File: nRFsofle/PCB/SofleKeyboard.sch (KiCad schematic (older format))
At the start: 106 parts, among them J1 LED, J2 4PIN, J3 OLED, J4 key leds, J5 backlight sel, J6 indicator bypass, J7 JST_Micro_2, J8 OLED, P1 i2c_pin, P2 i2c_pin, SW1 SW_PUSH-MX_W_LED, SW10 SW_PUSH-MX_W_LED, SW11 SW_PUSH-MX_W_LED, SW12 SW_PUSH-MX_W_LED, SW13 SW_PUSH-MX_W_LED, SW14 SW_PUSH-MX_W_LED, SW15 SW_PUSH-MX_W_LED, SW16 SW_PUSH-MX_W_LED, SW17 SW_PUSH-MX_W_LED, SW18 SW_PUSH-MX_W_LED, SW19 SW_PUSH-MX_W_LED, SW2 SW_PUSH-MX_W_LED, SW20 SW_PUSH-MX_W_LED, SW21 SW_PUSH-MX_W_LED, SW22 SW_PUSH-MX_W_LED, SW23 SW_PUSH-MX_W_LED, SW24 SW_PUSH-MX_W_LED, SW25 Rotary_Encoder_Switch, SW26 SW_PUSH-MX_W_LED, SW27 SW_PUSH-MX_W_LED, SW28 SW_PUSH-MX_W_LED, SW29 SW_PUSH-MX_W_LED, SW3 SW_PUSH-MX_W_LED, SW30 SW_PUSH-MX_W_LED, SW31 SPDT_Switch, SW4 SW_PUSH-MX_W_LED, SW5 SW_PUSH-MX_W_LED, SW6 SW_PUSH-MX_W_LED, SW7 SW_PUSH-MX_W_LED, SW8 SW_PUSH-MX_W_LED, SW9 SW_PUSH-MX_W_LED, U1 nRFMicro

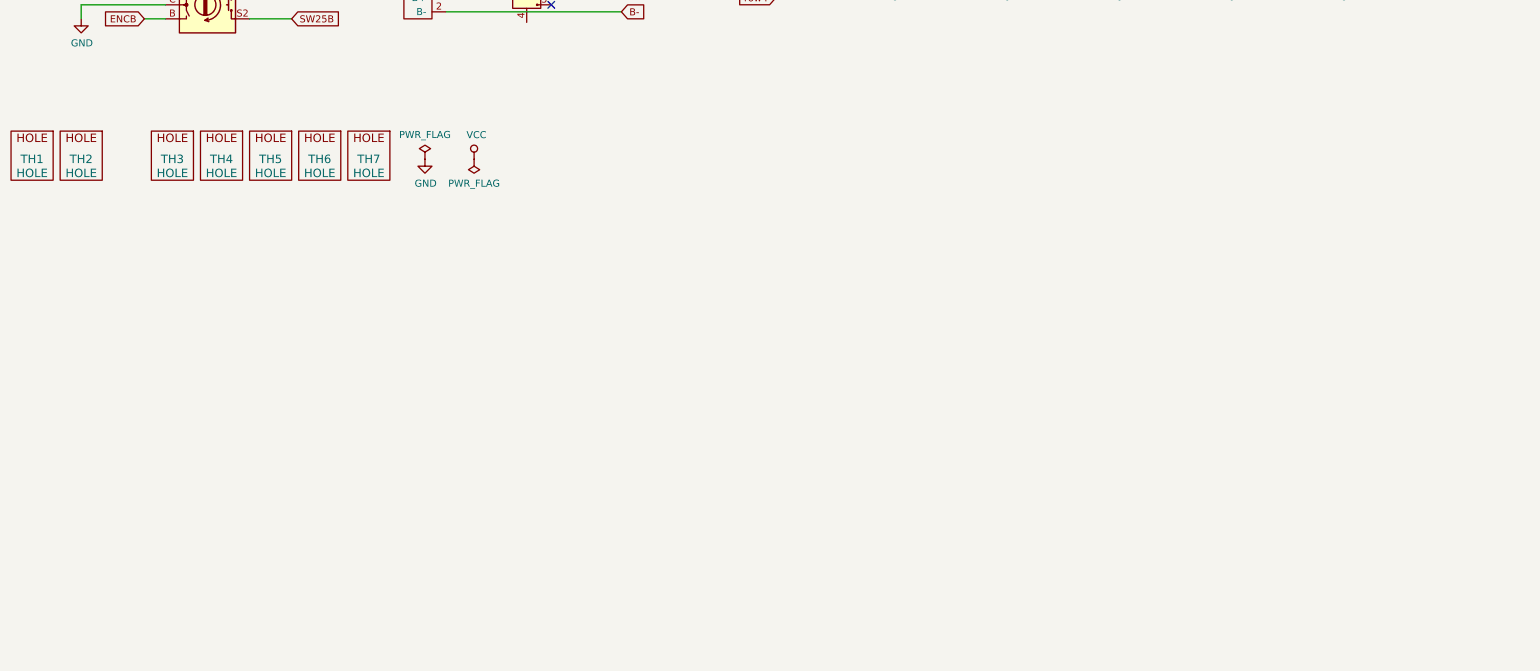
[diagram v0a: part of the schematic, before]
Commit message: Implemented the schematic to add fingerprint sensor
The implemented circuit is duplicated to put the circuit in both layers,
so the board can be printed for both sides of the keyboard.
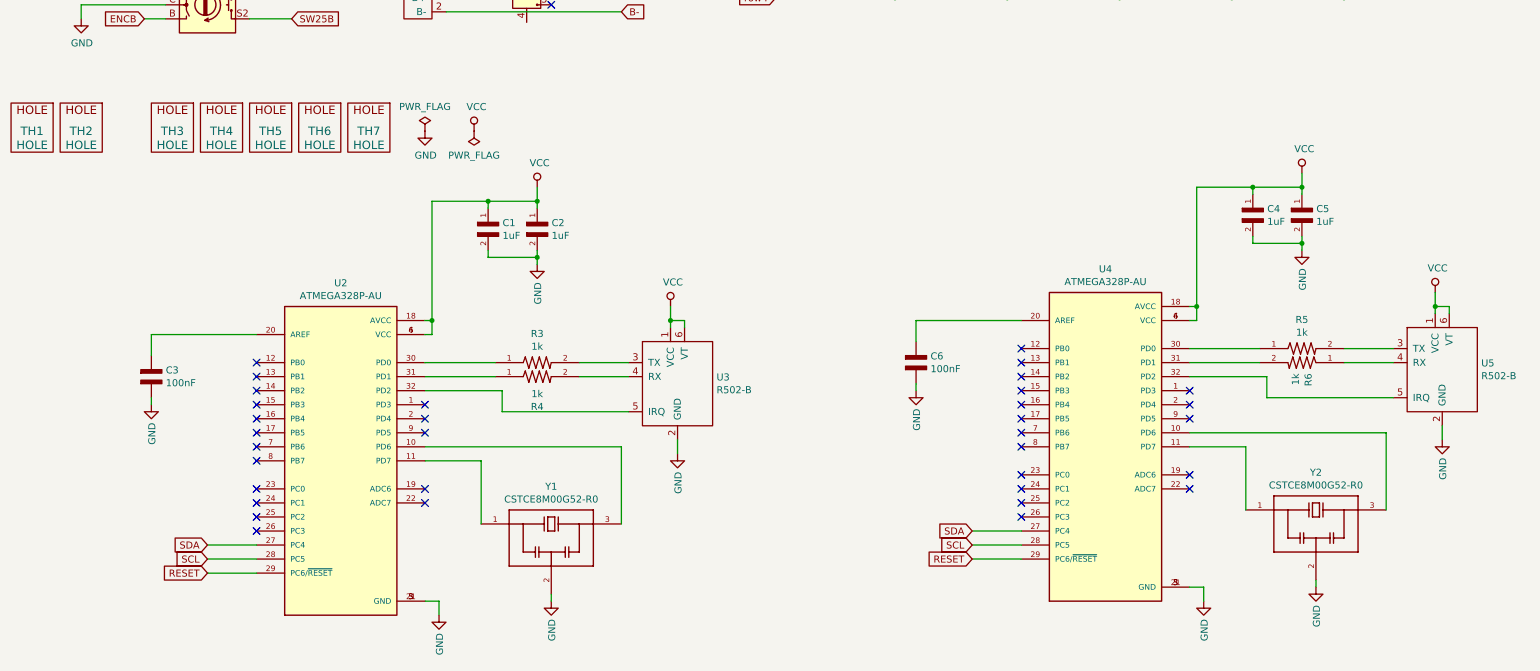
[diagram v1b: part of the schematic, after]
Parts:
- added C1, C2, C4, C5: 1uF, 1uF, symbol Additions:1uF
- added C3, C6: 100nF, 100nF, symbol Additions:100nF
- added R3, R4, R5, R6: 1k, 1k, symbol Additions:1k
- added U2, U4: ATMEGA328P-AU, QFP80P900X900X120-32N, symbol Additions:ATMEGA328P-AU
- added U3, U5: R502-B, symbol Additions:R502-B
- added Y1, Y2: CSTCE8M00G52-R0, OSC_CSTCE8M00G52-R0, symbol Additions:CSTCE8M00G52-R0
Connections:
- net GND: now also C1.2, C2.2, C3.1, C4.2, C5.2, C6.1, U2.21 (GND), U2.3 (GND), U2.5 (GND), U3.2 (GND), U4.21 (GND), U4.3 (GND), U4.5 (GND), U5.2 (GND), Y1.2, Y2.2
- net RESET: now also U2.29 (PC6/~RESET), U4.29 (PC6/~RESET)
- net SCL: now also U2.28 (PC5), U4.28 (PC5)
- net SDA: now also U2.27 (PC4), U4.27 (PC4)
- net VCC: now also C1.1, C2.1, C4.1, C5.1, U2.18 (AVCC), U2.4 (VCC), U2.6 (VCC), U3.1 (VCC), U3.6 (VT), U4.18 (AVCC), U4.4 (VCC), U4.6 (VCC), U5.1 (VCC), U5.6 (VT)
- new net: U2.10 (PD6), Y1.3
- new net: U2.11 (PD7), Y1.1
- new net: C3.2, U2.20 (AREF)
- new net: R3.1, U2.30 (PD0)
- new net: R4.1, U2.31 (PD1)
- new net: U2.32 (PD2), U3.5 (IRQ)
- new net: R3.2, U3.3 (TX)
- new net: R4.2, U3.4 (RX)
- new net: C6.2, U4.20 (AREF)
- new net: U4.11 (PD7), Y2.1
- new net: U4.10 (PD6), Y2.3
- new net: R6.1, U5.4 (RX)
- new net: R6.2, U4.31 (PD1)
- new net: R5.1, U4.30 (PD0)
- new net: R5.2, U5.3 (TX)
- new net: U4.32 (PD2), U5.5 (IRQ)
- no-connect marks 5 -> 39
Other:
- moved on the sheet: TH1, TH2, TH3, TH4, TH5, TH6, TH7

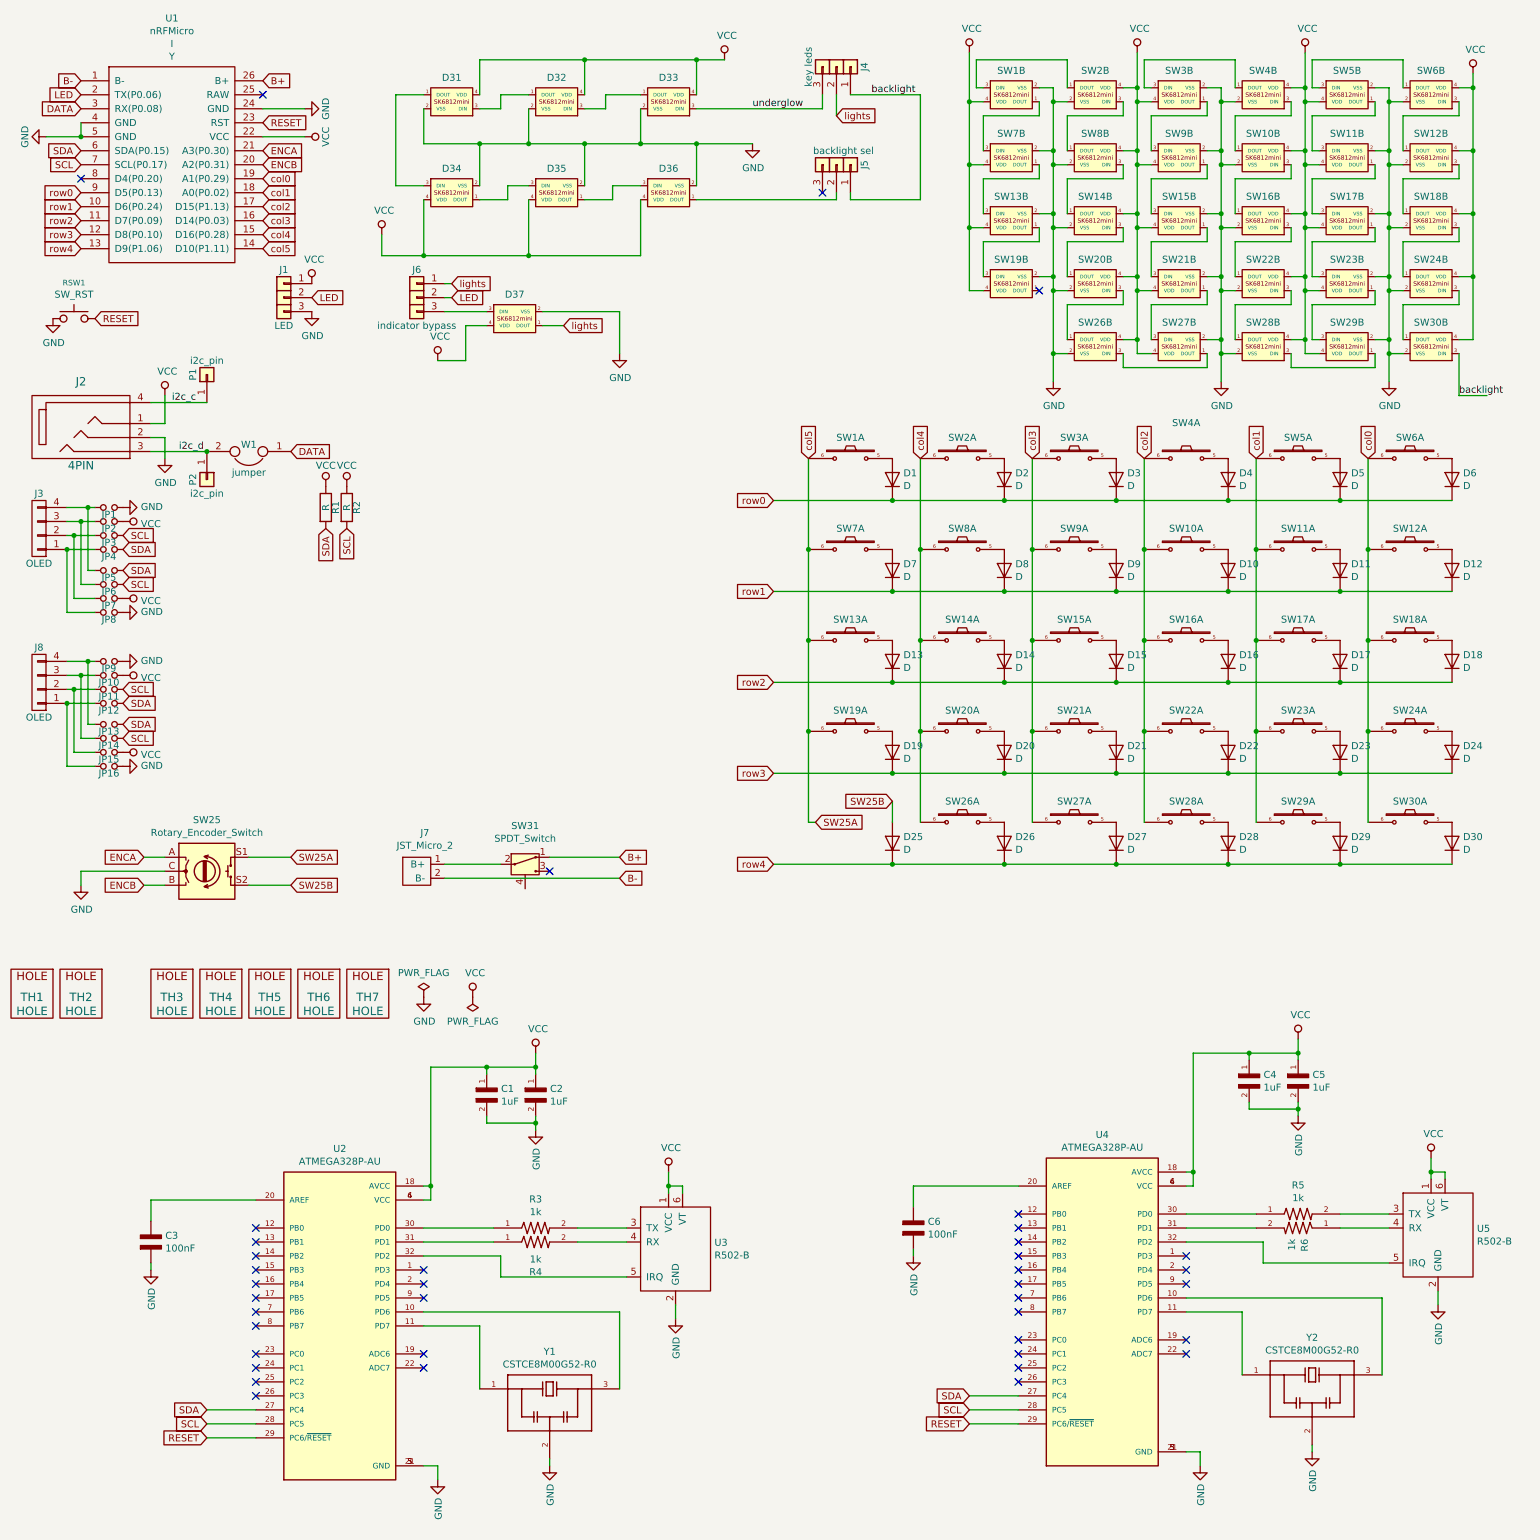
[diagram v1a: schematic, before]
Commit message: Generated the PCB to add fingerprint sensor to the keyboard
In order to add this new feature, a microcontroller was added.
It is duplicated because this board can be used as left and
right sides of the keyboard, so only one of the sides should
be soldered.

The Atmega microcontroller reads the fingerprint sensor using
UART protocol while the nRFmicro reads the Arduino fingerprint
sensor read data using I2C sensor. An additional wire was added
between the Atmega and the nRFmicro to the Atmega be able to
interrupt the nRFmicro every time the fingerprint sensor detects a
finger.
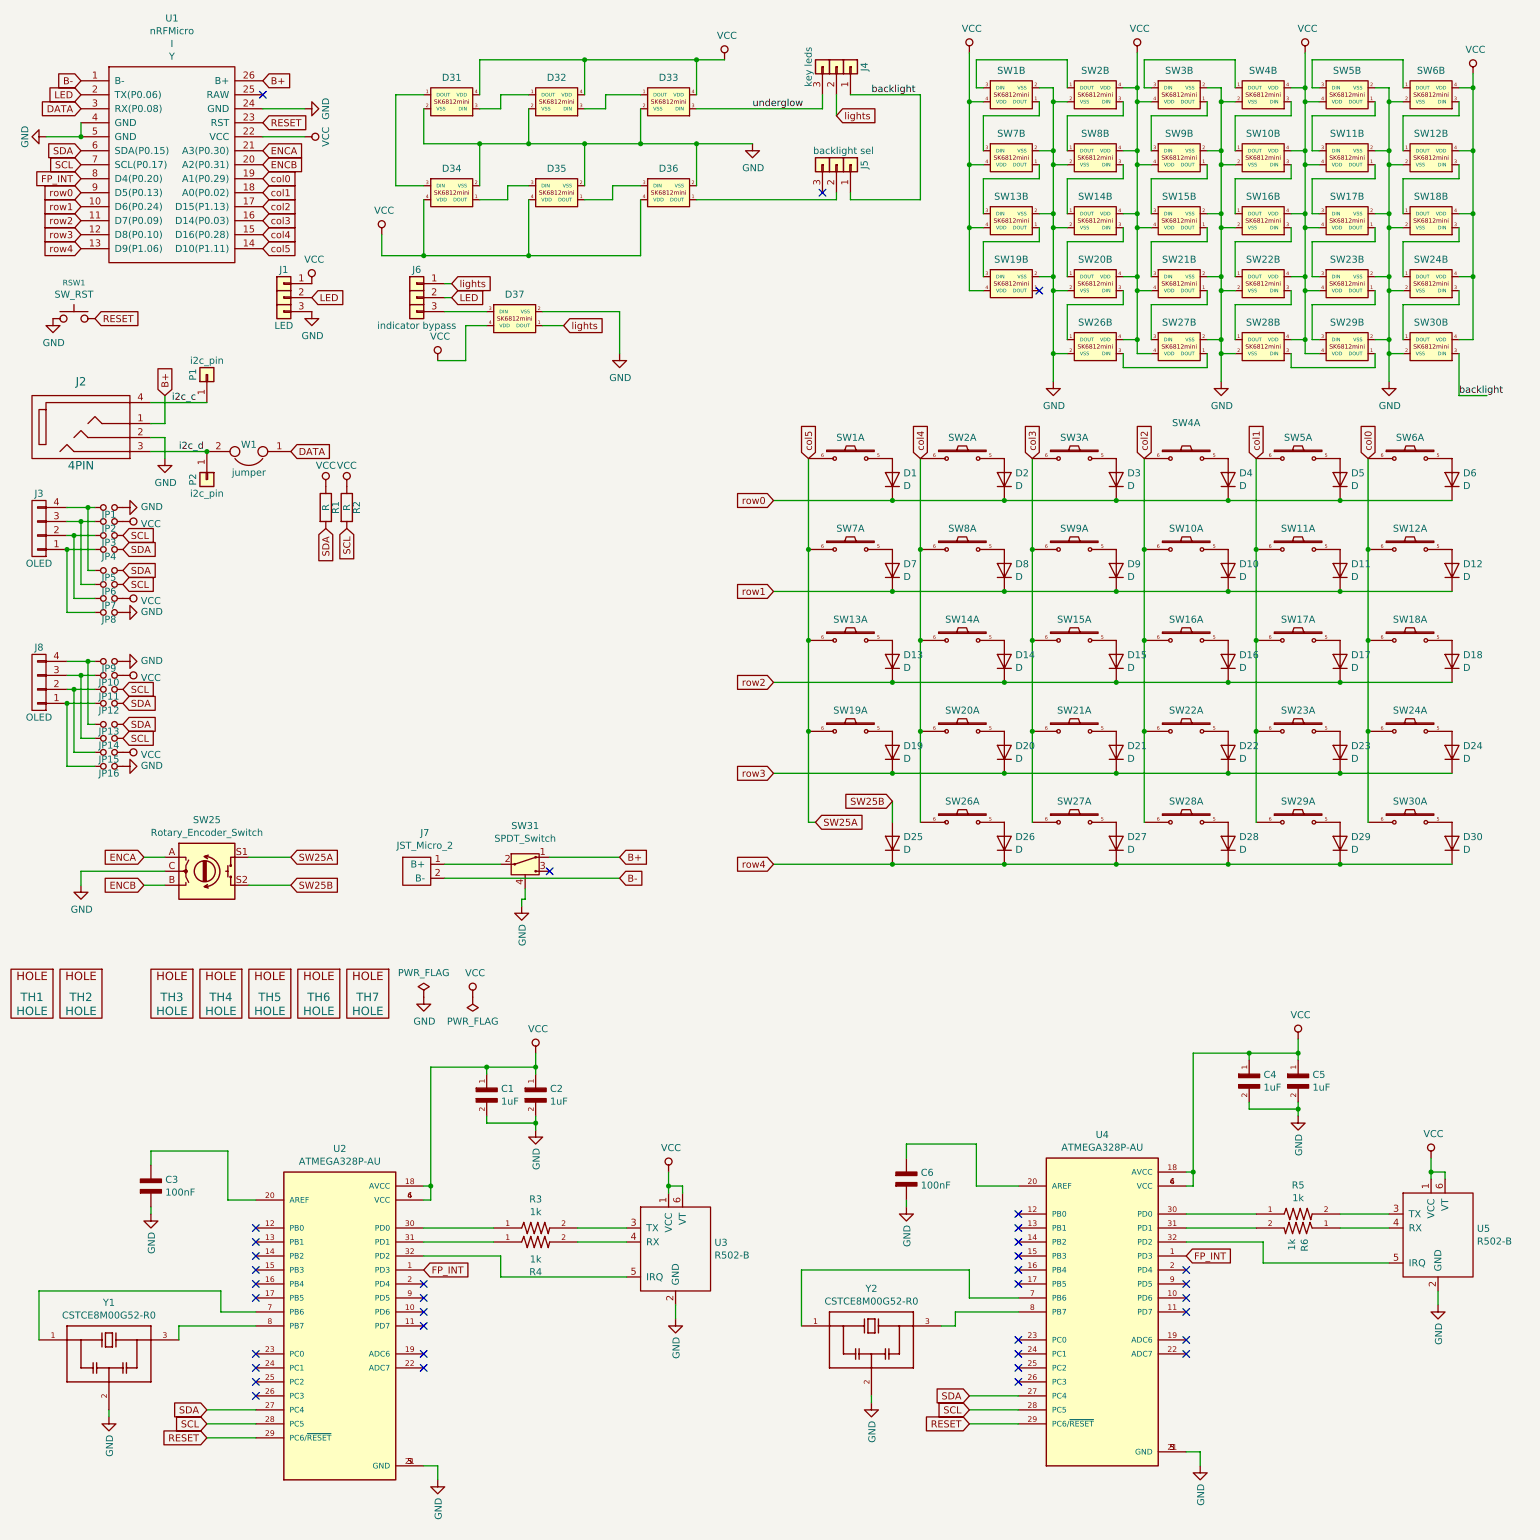
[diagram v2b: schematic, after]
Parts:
- C1, C2, C4, C5: footprint 1uF -> Additions:1uF
- C3, C6: footprint 100nF -> Additions:100nF
- R3, R4, R5, R6: footprint 1k -> Additions:1k
- U2, U4: footprint QFP80P900X900X120-32N -> Additions:QFP80P900X900X120-32N
- U3, U5: footprint (none) -> Additions:R502-B
- Y1, Y2: footprint OSC_CSTCE8M00G52-R0 -> Additions:OSC_CSTCE8M00G52-R0
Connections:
- net B+: now also J2.1
- net GND: now also SW31.4
- net VCC: no longer J2.1
- net FP_INT: now reaches U1.8 (D4(P0.20))
- net FP_INT: now also U2.1 (PD3), U4.1 (PD3)
- net at U2.10 (PD6): no longer Y1.3
- net at U2.11 (PD7): no longer Y1.1
- net at U2.7 (PB6): now also Y1.1
- net at U2.8 (PB7): now also Y1.3
- net at Y2.1: now also U4.7 (PB6); no longer U4.11 (PD7)
- net at Y2.3: now also U4.8 (PB7); no longer U4.10 (PD6)
- no-connect marks 39 -> 36
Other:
- moved on the sheet: C3, C6, Y1, Y2

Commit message: Added SPI programmer port interface
Pinout of this port is equal to the used by Arduino Nano
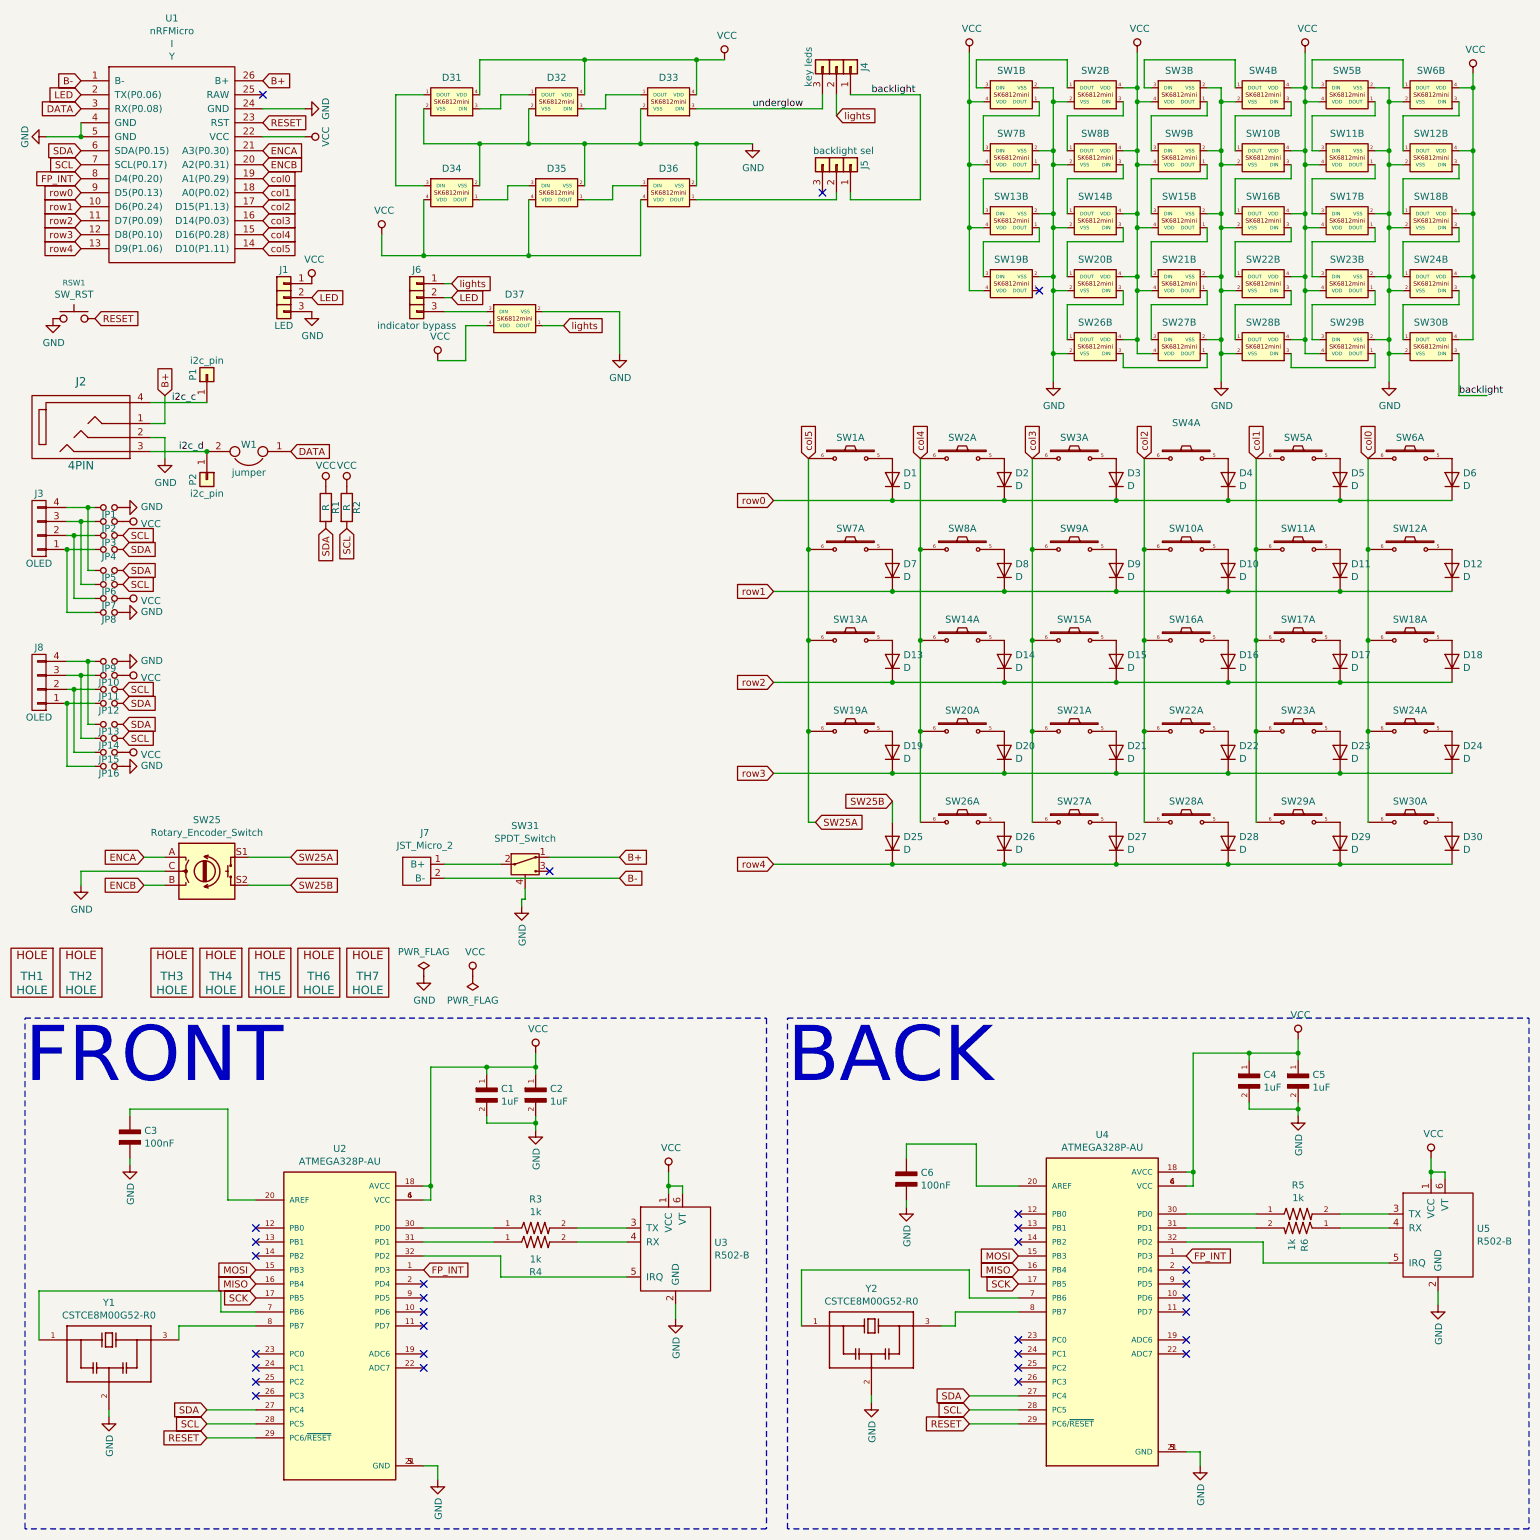
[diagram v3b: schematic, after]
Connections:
- net MOSI: now reaches U2.15 (PB3)
- net MOSI: now also U4.15 (PB3)
- net MISO: now reaches U2.16 (PB4)
- net MISO: now also U4.16 (PB4)
- net SCK: now reaches U2.17 (PB5)
- net SCK: now also U4.17 (PB5)
- no-connect marks 36 -> 30
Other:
- note added: "BACK"
- note added: "FRONT"
- moved on the sheet: C3, TH1, TH2, TH3, TH4, TH5, TH6, TH7
